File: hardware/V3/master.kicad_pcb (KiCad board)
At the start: 4 copper layers, 40 x 40 mm, 118 parts, among them J1 USB-C, J2 DRILL, J3 DRILL, J4 DRILL, J5 DRILL, J6 STACK-UP-LOW, J7 STACK-DOWN, J8 STACK-UP-LOW, J9 STACK-DOWN, P1 Port A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

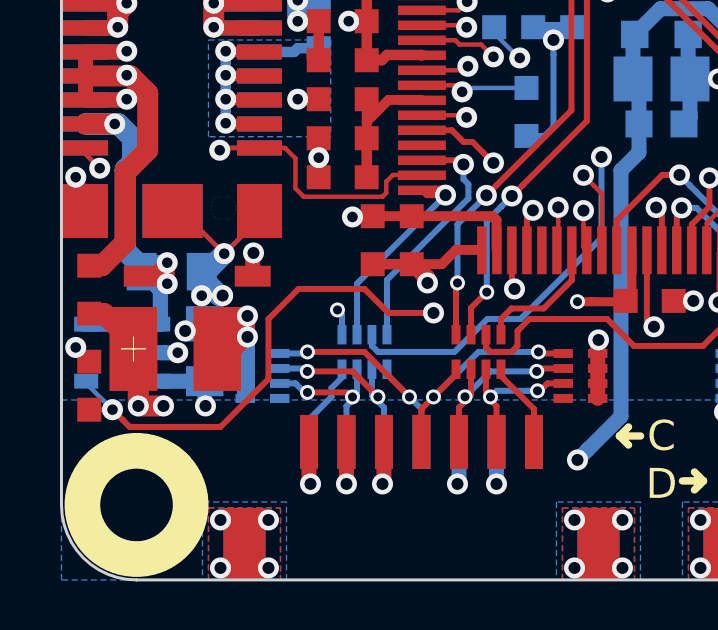
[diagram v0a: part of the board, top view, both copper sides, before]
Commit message: changed Stack 3v3 driver. Ordered Prototype
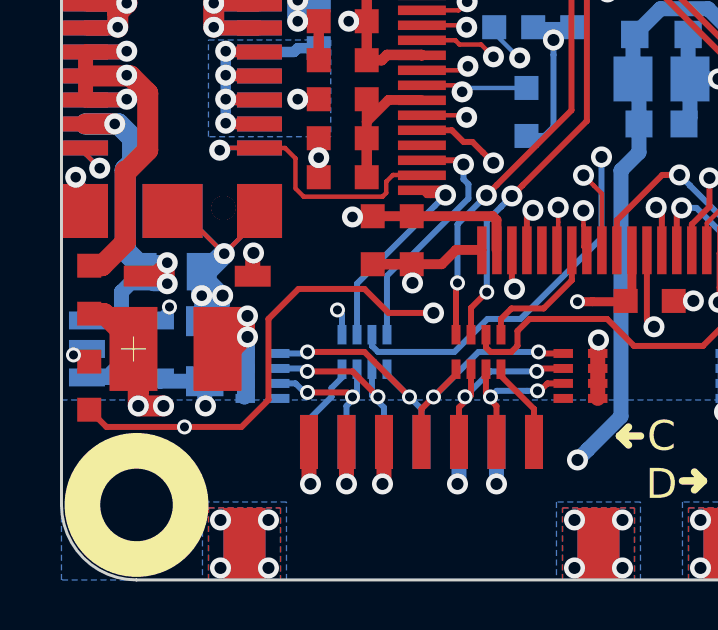
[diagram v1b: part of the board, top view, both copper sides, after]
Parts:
- U13: value RT9701XB -> STMPS2171STR; footprint SOT23-5 -> kicad-libraries:SOT23-5L
- moved U13 0.13 mm to (127.0, 102.3)
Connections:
- U13 pad 3: 3V3 -> Net-(U13-Pad3)
- U13 pad 5: VCC -> 3V3
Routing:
- net 3V3-EN: track 22.4 -> 25.9 mm, vias 3 -> 4
- net VCC: track 27.4 -> 24.1 mm
- net GND: track 199.8 -> 200.7 mm, vias 79 -> 77

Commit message: Added logo "CE" and "WEEE", added testpionts for bricklet 3,3V and 5V, added second CC resistor.
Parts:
- added P8: Bricklet 5V, kicad-libraries:TSTPT, B.Cu at (148.4, 94.2)
- added P9: Bricklet 3,3V, kicad-libraries:TSTPT, B.Cu at (148.4, 96.1)
- added R18: 56k, kicad-libraries:R0603F, B.Cu at (140.7, 74.7)
- added VAL: WEEE_7mm, kicad-libraries:WEEE_7mm, B.Cu at (142.0, 99.8)
- added VAL: CE_5mm, kicad-libraries:CE_5mm, B.Cu at (136.3, 99.2)
- U1: value AT91SAM3SXC -> SAM???
- U4: value AP7333-33SAG -> AP7333-33SRG
- U5: value DNP -> AP7333-33SRG
- moved G*** 15.5 mm to (138.1, 84.9)
- moved R5 4.35 mm to (145.0, 74.7)
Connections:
- J1 pad 5: GND -> Net-(J1-Pad5)
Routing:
- net Net-(FB1-Pad2): track 21.1 -> 26.3 mm
- net 3,3VBricklet: track 24.8 -> 29.5 mm
- net Net-(J1-Pad4): track 8.43 -> 4.04 mm
- net Net-(J1-Pad5): track 0.00 -> 4.00 mm, vias 0 -> 1
- net 5VBricklet: track 32.8 -> 35.6 mm
- net GND: track 200.7 -> 199.0 mm, vias 77 -> 76
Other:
- board text added: "B3V3"
- board text added: "B5V"

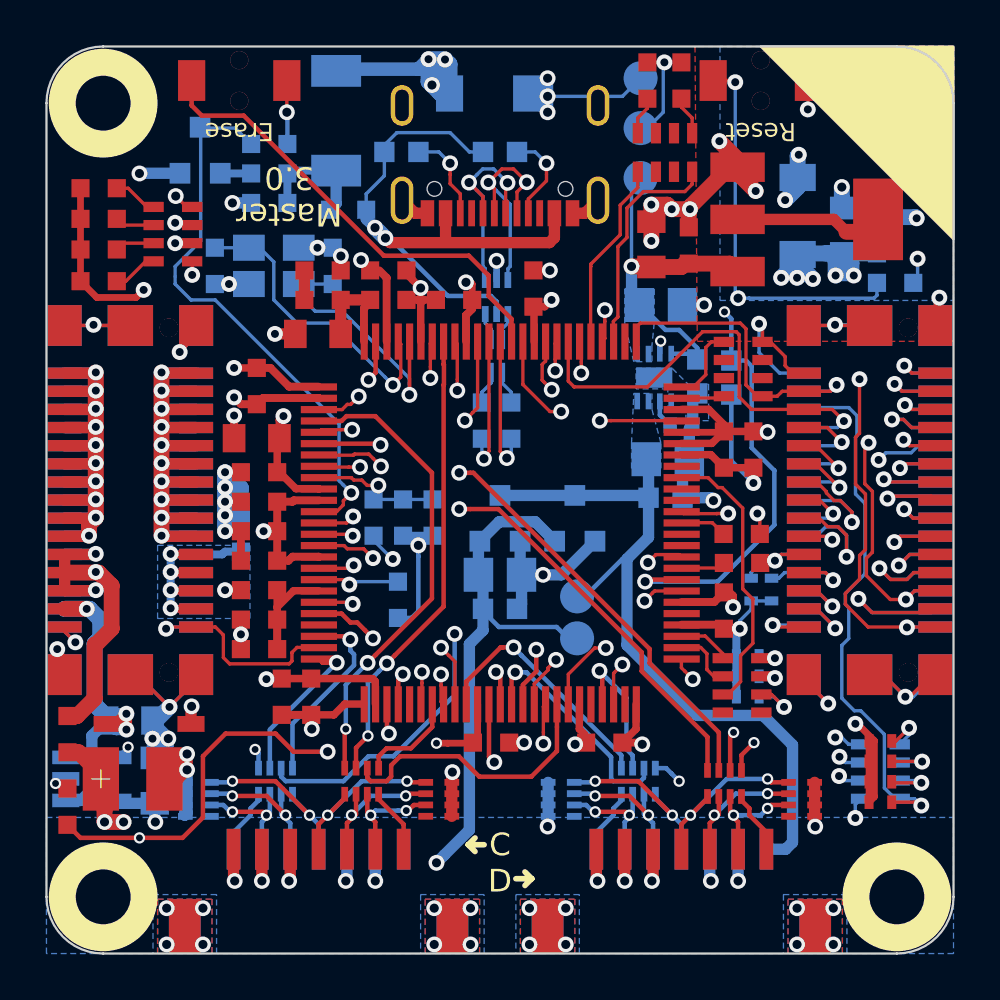
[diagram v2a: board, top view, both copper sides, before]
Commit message: added filter
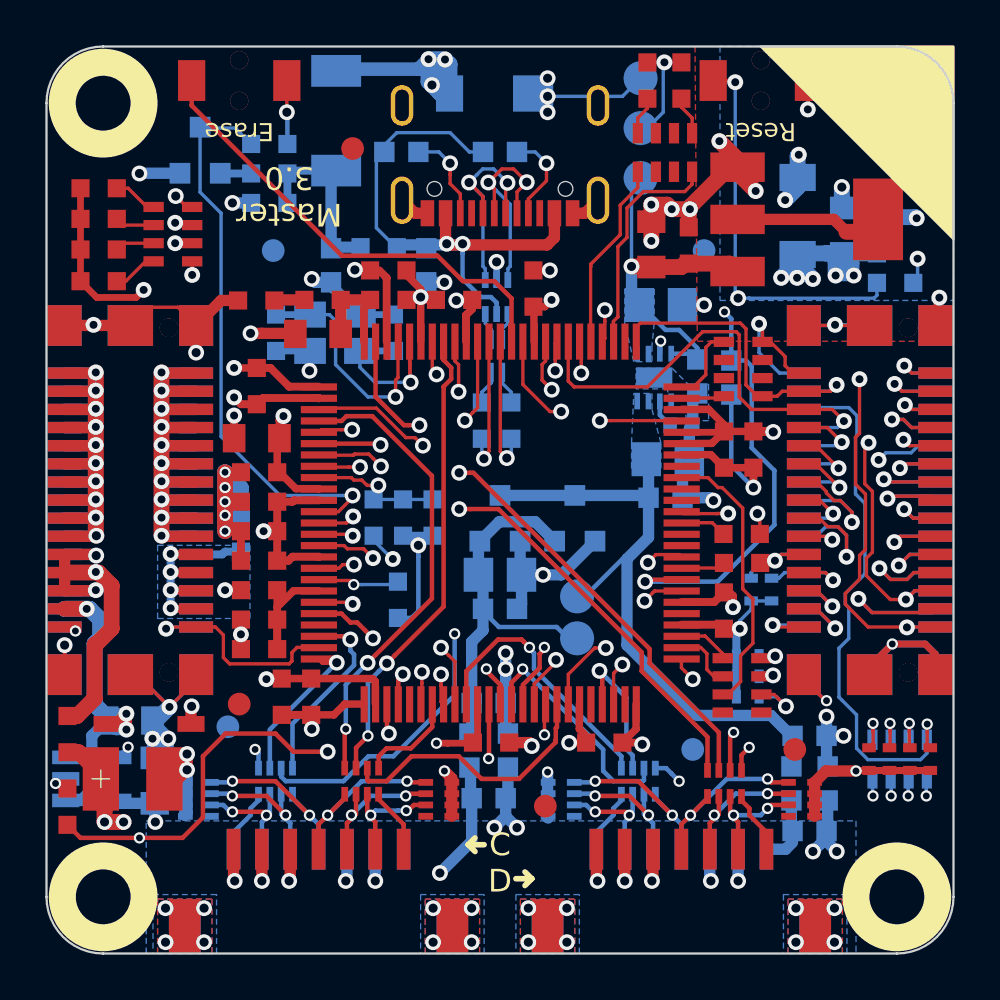
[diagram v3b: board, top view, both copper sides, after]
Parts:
- added C46: TBD, kicad-libraries:C0603F, B.Cu at (137.6, 79.7)
- added C47: TBD, kicad-libraries:C0603F, B.Cu at (141.8, 79.7)
- added C48: TBD, kicad-libraries:C0603F, B.Cu at (158.7, 104.6)
- added C49: TBD, kicad-libraries:C0603F, B.Cu at (158.7, 100.4)
- added C50: TBD, kicad-libraries:C0603F, B.Cu at (144.5, 99.0)
- added C51: TBD, kicad-libraries:C0603F, B.Cu at (144.5, 103.2)
- added Fiducial_Mark: VAL**, kicad-libraries:Fiducial_Mark, B.Cu at (153.5, 101.0)
- added Fiducial_Mark: VAL**, kicad-libraries:Fiducial_Mark, B.Cu at (133.0, 100.0)
- added Fiducial_Mark: VAL**, kicad-libraries:Fiducial_Mark, B.Cu at (154.0, 79.0)
- added Fiducial_Mark: VAL**, kicad-libraries:Fiducial_Mark, B.Cu at (135.0, 79.0)
- added Fiducial_Mark: VAL**, kicad-libraries:Fiducial_Mark, F.Cu at (133.5, 99.0)
- added Fiducial_Mark: VAL**, kicad-libraries:Fiducial_Mark, F.Cu at (147.0, 103.5)
- added Fiducial_Mark: VAL**, kicad-libraries:Fiducial_Mark, F.Cu at (158.0, 101.0)
- added Fiducial_Mark: VAL**, kicad-libraries:Fiducial_Mark, F.Cu at (138.5, 74.5)
- added L3: FB, kicad-libraries:R0603F, B.Cu at (157.8, 102.5)
- added L4: FB, kicad-libraries:R0603F, B.Cu at (143.7, 101.0)
- added L5: FB, kicad-libraries:R0603F, B.Cu at (159.4, 102.5)
- added L6: FB, kicad-libraries:R0603F, B.Cu at (145.3, 101.0)
- moved VAL 12.5 mm to (137.4, 86.7)
- moved G*** 10.7 mm to (129.9, 78.0)
- moved VAL 5.53 mm to (137.4, 96.7)
- moved C12 4.00 mm to (140.3, 82.6)
- moved C13 4.00 mm to (135.1, 82.6)
- moved X1 4.00 mm to (137.7, 82.6)
- moved C36 3.21 mm to (134.2, 81.2), turned to 180 degrees
- moved C3 2.91 mm to (164.0, 101.4), turned to 270 degrees
- moved FB1 2.13 mm to (139.7, 78.8)
- moved C5 1.64 mm to (163.1, 101.4), turned to 270 degrees
- moved RP1 1.01 mm to (162.6, 101.4), turned to 0 degrees
- moved C9 0.94 mm to (161.3, 101.4), turned to 270 degrees
- moved C7 0.41 mm to (162.2, 101.4), turned to 270 degrees
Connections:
- C41 pad 2: 5VBricklet -> Net-(C41-Pad2)
- C42 pad 2: 5VBricklet -> Net-(C41-Pad2)
- C43 pad 2: 3,3VBricklet -> Net-(C43-Pad2)
- C44 pad 2: 3,3VBricklet -> Net-(C43-Pad2)
- P1 pad 2: GND -> GNDD1
- P1 pad EP: GND -> GNDD1
- P2 pad 2: GND -> GNDD1
- P2 pad EP: GND -> GNDD1
- P3 pad 2: GND -> GNDD1
- P3 pad EP: GND -> GNDD1
- P4 pad 2: GND -> GNDD1
- P4 pad EP: GND -> GNDD1
- P8 pad 1: 5VBricklet -> Net-(C41-Pad2)
- P9 pad 1: 3,3VBricklet -> Net-(C43-Pad2)
- U3 pad 7: 5VBricklet -> Net-(C41-Pad2)
- U3 pad 8: 5VBricklet -> Net-(C41-Pad2)
- U4 pad 2: 3,3VBricklet -> Net-(C43-Pad2)
- U4 pad 3: 5VBricklet -> Net-(C41-Pad2)
- U5 pad 2: 3,3VBricklet -> Net-(C43-Pad2)
- U5 pad 3: 5VBricklet -> Net-(C41-Pad2)
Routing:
- net 5VBricklet: track 35.6 -> 5.49 mm
- net Net-(C41-Pad2): track 0.00 -> 28.5 mm
- net 3V3: track 105.5 -> 78.3 mm
- net 3,3VBricklet: track 29.5 -> 10.9 mm
- net Net-(C43-Pad2): track 0.00 -> 17.5 mm
- net GNDD1: track 0.00 -> 12.8 mm, vias 0 -> 24
- net XOUT: track 13.8 -> 8.58 mm
- net Net-(RP1-Pad2): track 18.7 -> 22.8 mm
- net Net-(C27-Pad1): track 77.6 -> 73.9 mm
- net Net-(RP1-Pad3): track 23.8 -> 27.2 mm
- net Net-(RP1-Pad1): track 18.3 -> 21.6 mm
- net XIN: track 13.5 -> 10.4 mm
- net VUSB: track 5.16 -> 8.16 mm
- net LED3: track 22.1 -> 19.1 mm
- net LED4: track 25.7 -> 22.8 mm
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- added copper zone on B.Cu, net GNDD1
- added copper zone on F.Cu, net GNDD1
- added copper zone on GND, net GNDD1
- added copper zone on B.Cu, net Net-(C41-Pad2)
- removed copper zone on F.Cu, net GND
